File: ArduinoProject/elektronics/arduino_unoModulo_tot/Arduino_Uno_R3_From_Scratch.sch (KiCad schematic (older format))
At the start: 0 parts

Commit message: altered kicad
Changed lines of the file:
@@
 LIBS:MFN_STMicro
 LIBS:Arduino_Uno_R3_From_Scratch-cache
+LIBS:L298_Driver-cache
 EELAYER 25 0
 EELAYER END
 $Descr A4 11693 8268
 encoding utf-8
-Sheet 1 5
+Sheet 1 6
 Title "Arduino UNO R3 Clone"
 Date "8 oct 2015"
@@
 Wire Wire Line
 	7550 6150 7050 6150
+$Sheet
+S 2100 3500 1450 1200
+U 5A8D7699
+F0 "L298_Driver." 60
+F1 "L298_Driver.sch" 60
+$EndSheet
 $EndSCHEMATC

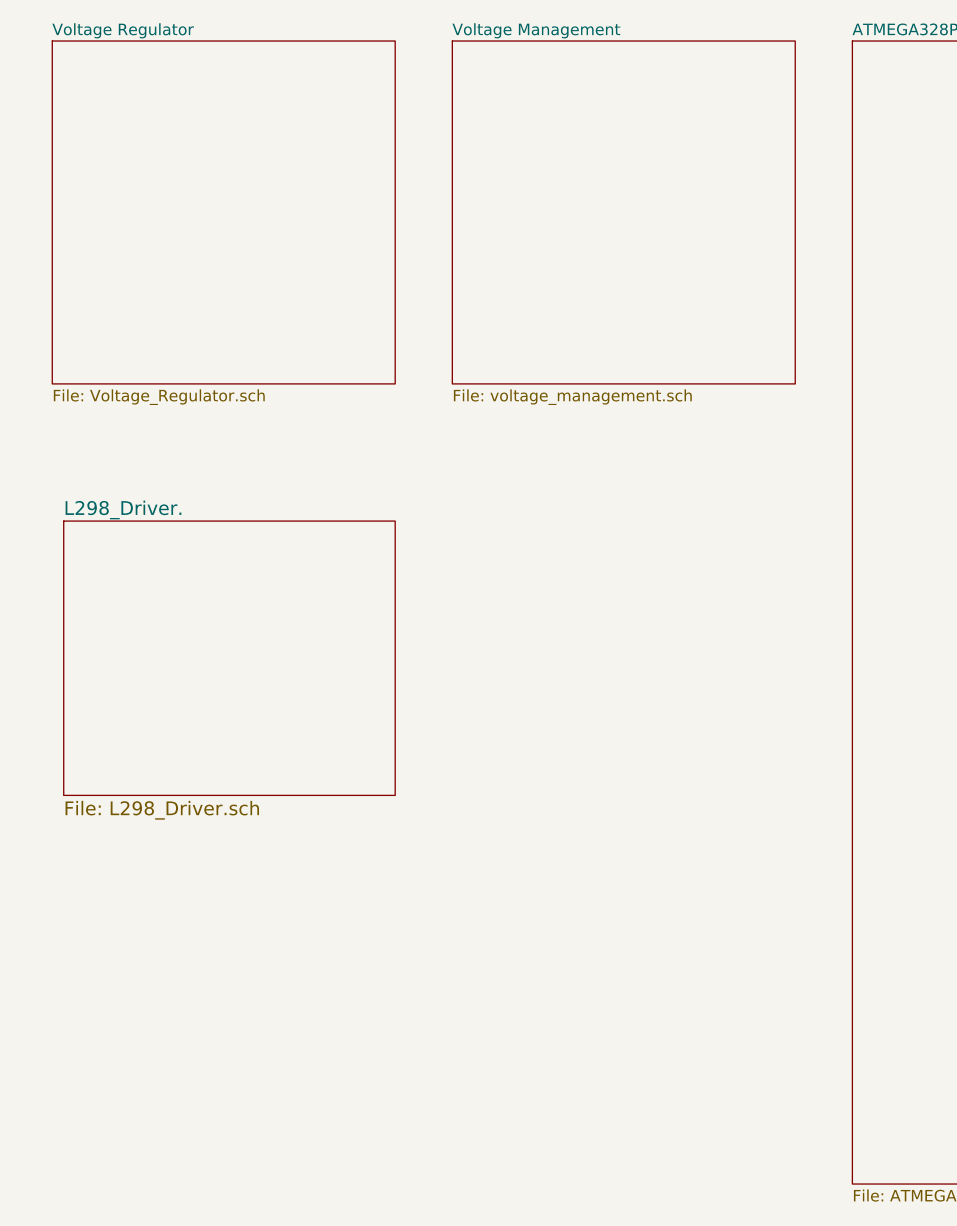
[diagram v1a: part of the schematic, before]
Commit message: kicad schema altered: alles op 1 PCB
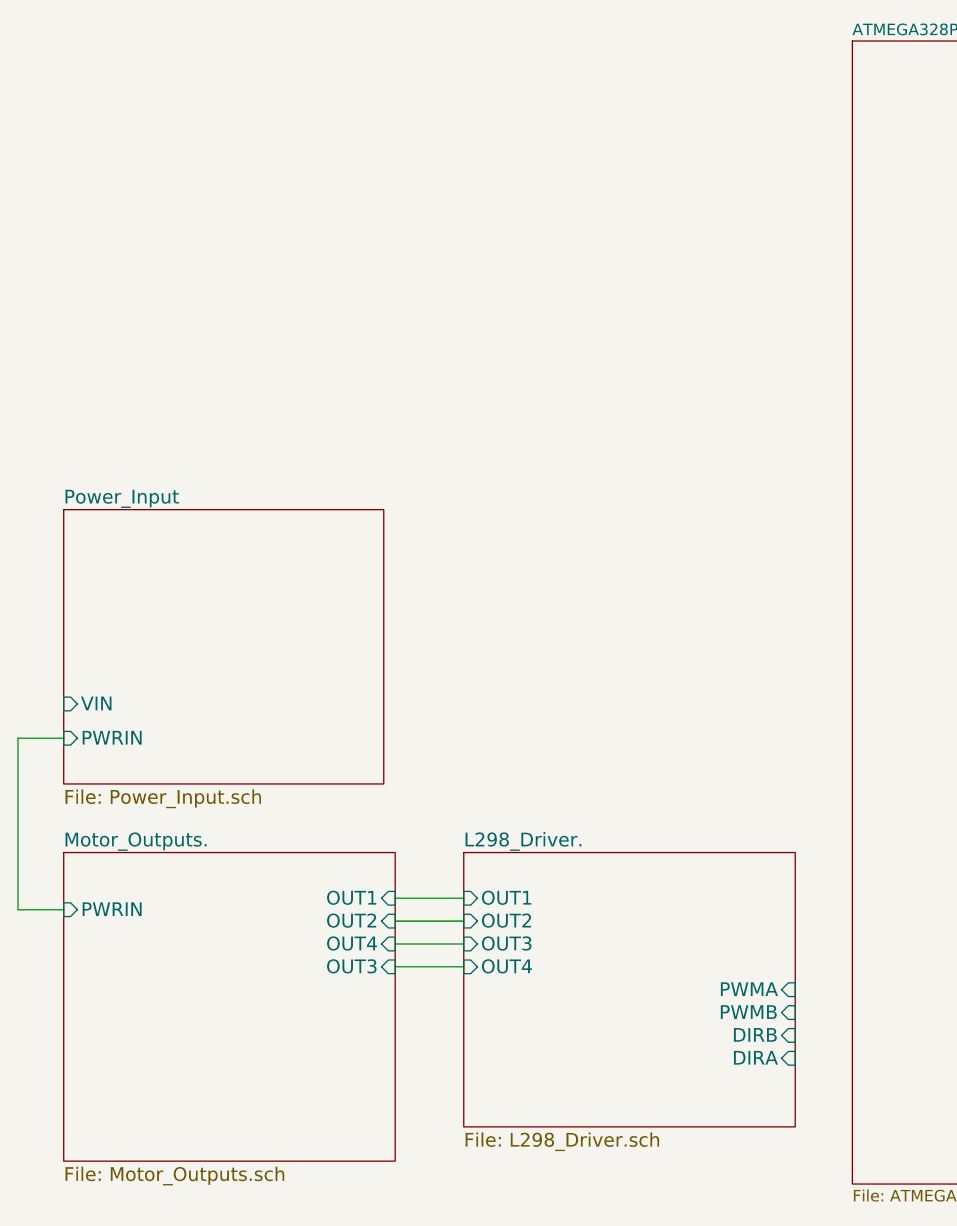
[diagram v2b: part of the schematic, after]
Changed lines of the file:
@@
 LIBS:MFN_STMicro
 LIBS:Arduino_Uno_R3_From_Scratch-cache
-LIBS:L298_Driver-cache
 EELAYER 25 0
 EELAYER END
@@
 Comment4 ""
 $EndDescr
-$Sheet
-S 2050 1400 1500 1500
-U 55CCFEA2
-F0 "Voltage Regulator" 50
-F1 "Voltage_Regulator.sch" 50
-$EndSheet
-$Sheet
-S 3800 1400 1500 1500
-U 55D0D7E6
-F0 "Voltage Management" 50
-F1 "voltage_management.sch" 50
-$EndSheet
 $Sheet
 S 7550 2400 1500 4000
@@
 	7550 6150 7050 6150
 $Sheet
-S 2100 3500 1450 1200
+S 3850 4950 1450 1200
 U 5A8D7699
 F0 "L298_Driver." 60
 F1 "L298_Driver.sch" 60
+F2 "OUT1" I L 3850 5150 60
+F3 "OUT2" I L 3850 5250 60
+F4 "OUT3" I L 3850 5350 60
+F5 "OUT4" I L 3850 5450 60
+F6 "PWMB" I R 5300 5650 60
+F7 "DIRB" I R 5300 5750 60
+F8 "DIRA" I R 5300 5850 60
+F9 "PWMA" I R 5300 5550 60
 $EndSheet
+$Sheet
+S 2100 3450 1400 1200
+U 5A965D0D
+F0 "Power_Input" 60
+F1 "Power_Input.sch" 60
+F2 "PWRIN" I L 2100 4450 60
+F3 "VIN" I L 2100 4300 60
+$EndSheet
+$Sheet
+S 2100 4950 1450 1350
+U 5A9679FD
+F0 "Motor_Outputs." 60
+F1 "Motor_Outputs.sch" 60
+F2 "OUT1" I R 3550 5150 60
+F3 "OUT2" I R 3550 5250 60
+F4 "OUT4" I R 3550 5350 60
+F5 "OUT3" I R 3550 5450 60
+F6 "PWRIN" I L 2100 5200 60
+$EndSheet
+Wire Wire Line
+	3550 5150 3850 5150
+Wire Wire Line
+	3550 5250 3850 5250
+Wire Wire Line
+	3550 5350 3850 5350
+Wire Wire Line
+	3550 5450 3850 5450
+Wire Wire Line
+	2100 4450 1900 4450
+Wire Wire Line
+	1900 4450 1900 5200
+Wire Wire Line
+	1900 5200 2100 5200
 $EndSCHEMATC

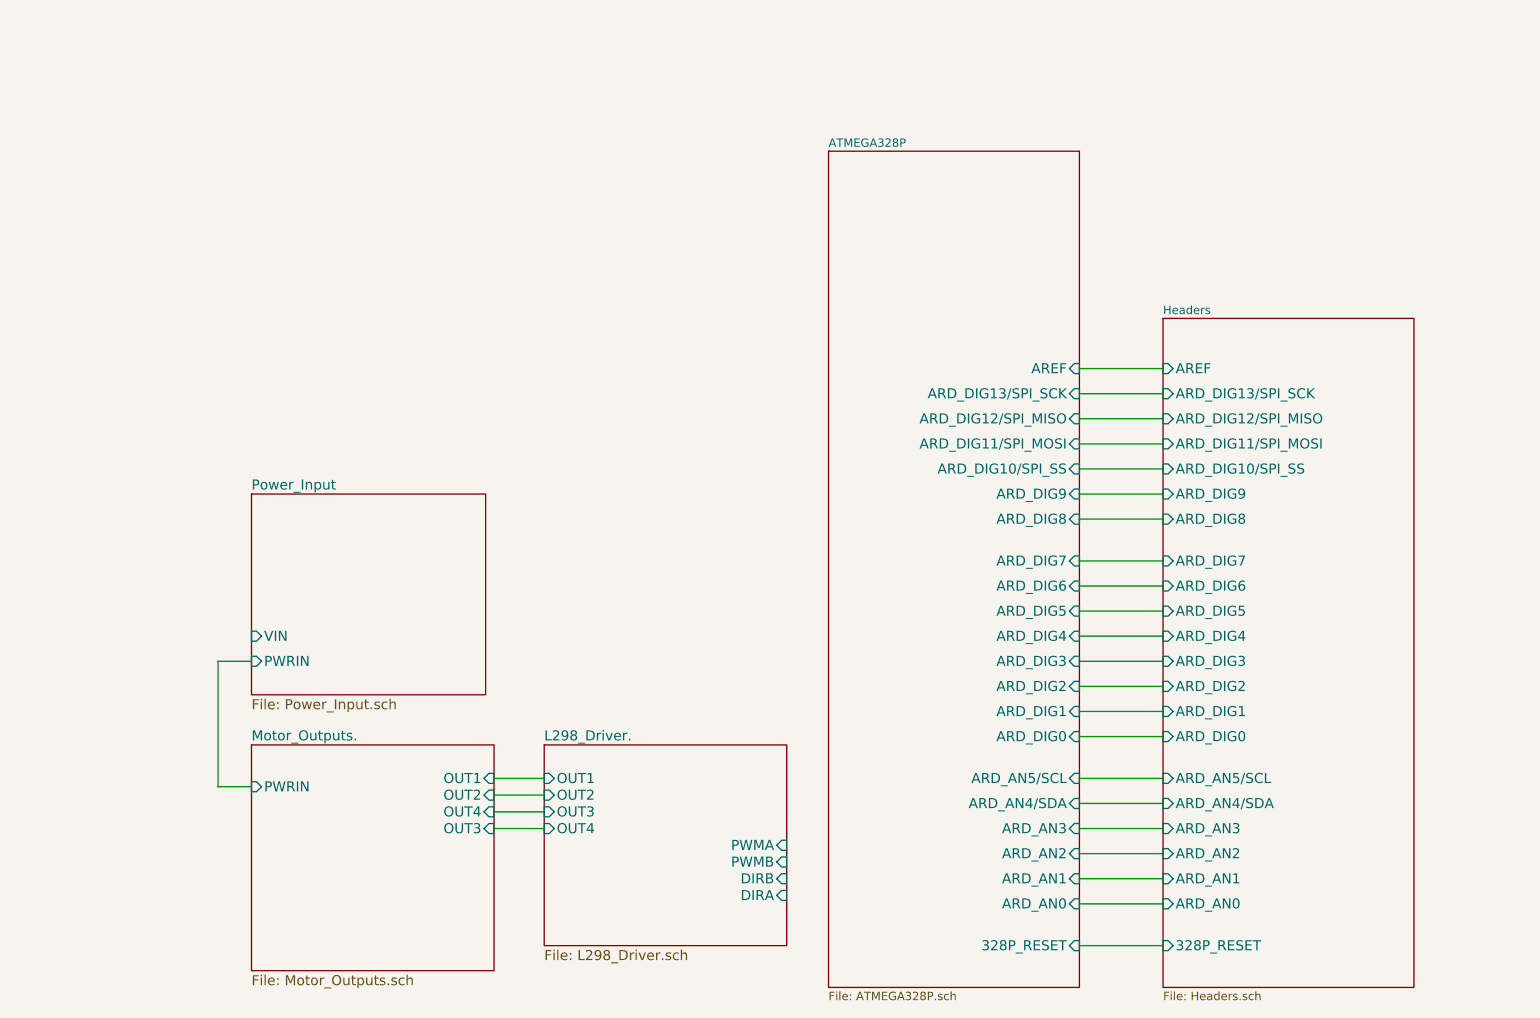
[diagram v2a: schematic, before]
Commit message: kicad schema altered: alles op 1 PCB2
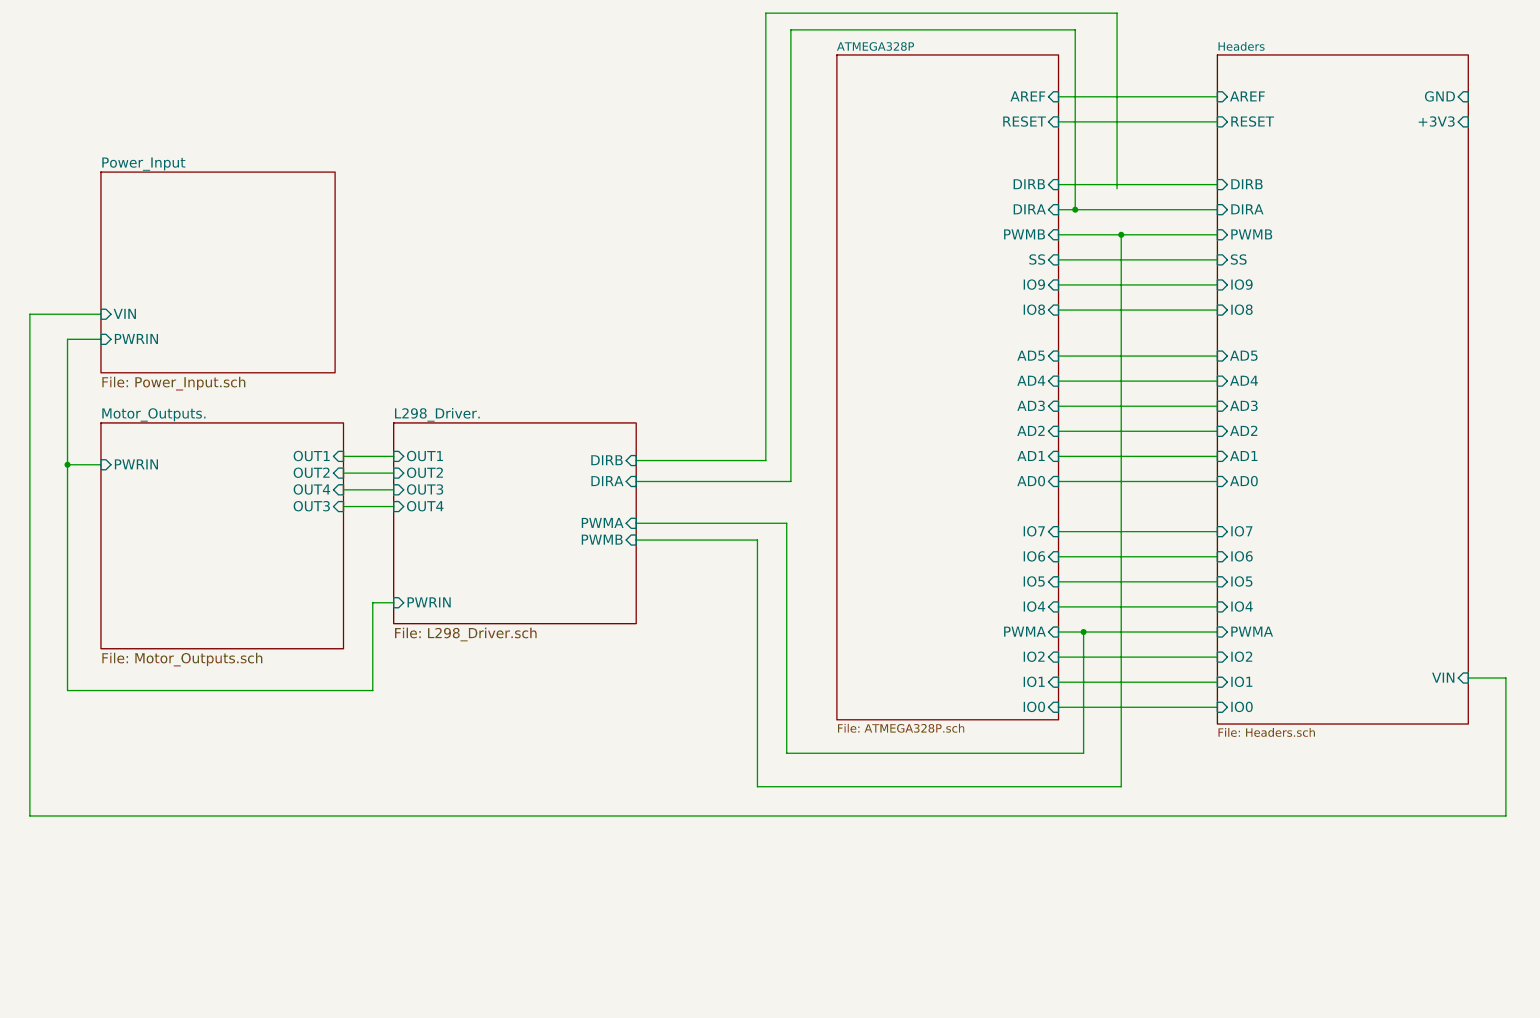
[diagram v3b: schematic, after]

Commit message: kicad schema altered: alles op 1 PCB3
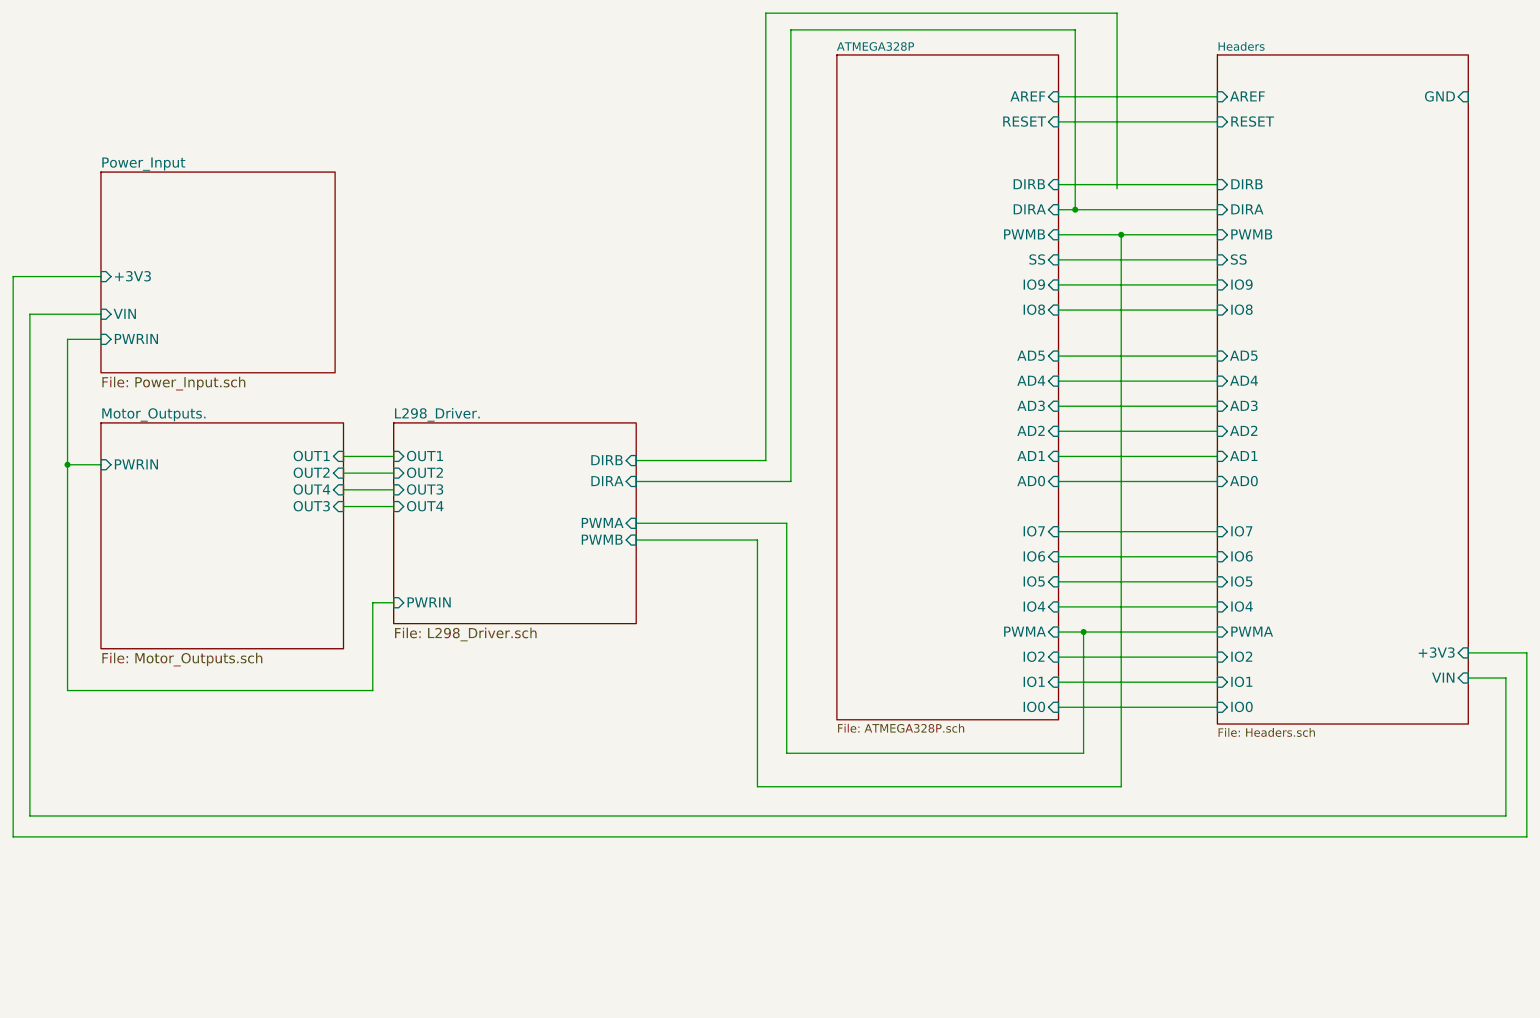
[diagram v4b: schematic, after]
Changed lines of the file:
@@
 F20 "IO9" I L 7875 2200 60
 F21 "IO8" I L 7875 2350 60
-F22 "+3V3" I R 9375 1225 60
+F22 "+3V3" I R 9375 4400 60
 F23 "RESET" I L 7875 1225 60
 F24 "VIN" I R 9375 4550 60
@@
 F2 "PWRIN" I L 1200 2525 60
 F3 "VIN" I L 1200 2375 60
+F4 "+3V3" I L 1200 2150 60
 $EndSheet
 $Sheet
@@
 	9600 4550 9600 5375
 Wire Wire Line
-	775  5375 9600 5375
+	9600 5375 775  5375
 Wire Wire Line
-	775  2375 775  5375
+	775  5375 775  2375
 Wire Wire Line
-	1200 2375 775  2375
+	775  2375 1200 2375
+Wire Wire Line
+	9375 4400 9725 4400
+Wire Wire Line
+	9725 4400 9725 5500
+Wire Wire Line
+	9725 5500 675  5500
+Wire Wire Line
+	675  5500 675  2150
+Wire Wire Line
+	675  2150 1200 2150
 $EndSCHEMATC
